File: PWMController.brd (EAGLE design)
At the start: 40 x 30 mm, 13 parts, among them IC1 LM555_DIP, Q1 BC337-25

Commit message: Adding updated files
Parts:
- D1, D2: value 1N4148 -> 1N4148DO35-7; device diode-1:DO35-10 -> diode:DO35-7
- D3: device SparkFun-LED:LED_5MM -> led:LED5MM
- turned J1 to 270 degrees
- turned J3 to 180 degrees
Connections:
- net GND: now also J1.2; no longer J1.1
- net N$1: now also J3.1; no longer J3.3
- net N$4: now also J3.3; no longer J3.1
- net VCC: now also J1.1; no longer J1.2
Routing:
- net V+: track 12.6 -> 14.9 mm
- net N$4: track 7.60 -> 8.87 mm
- net N$1: track 20.1 -> 21.1 mm
- net GND: track 64.9 -> 65.7 mm
- net THRESH_TRIG: track 24.3 -> 25.0 mm

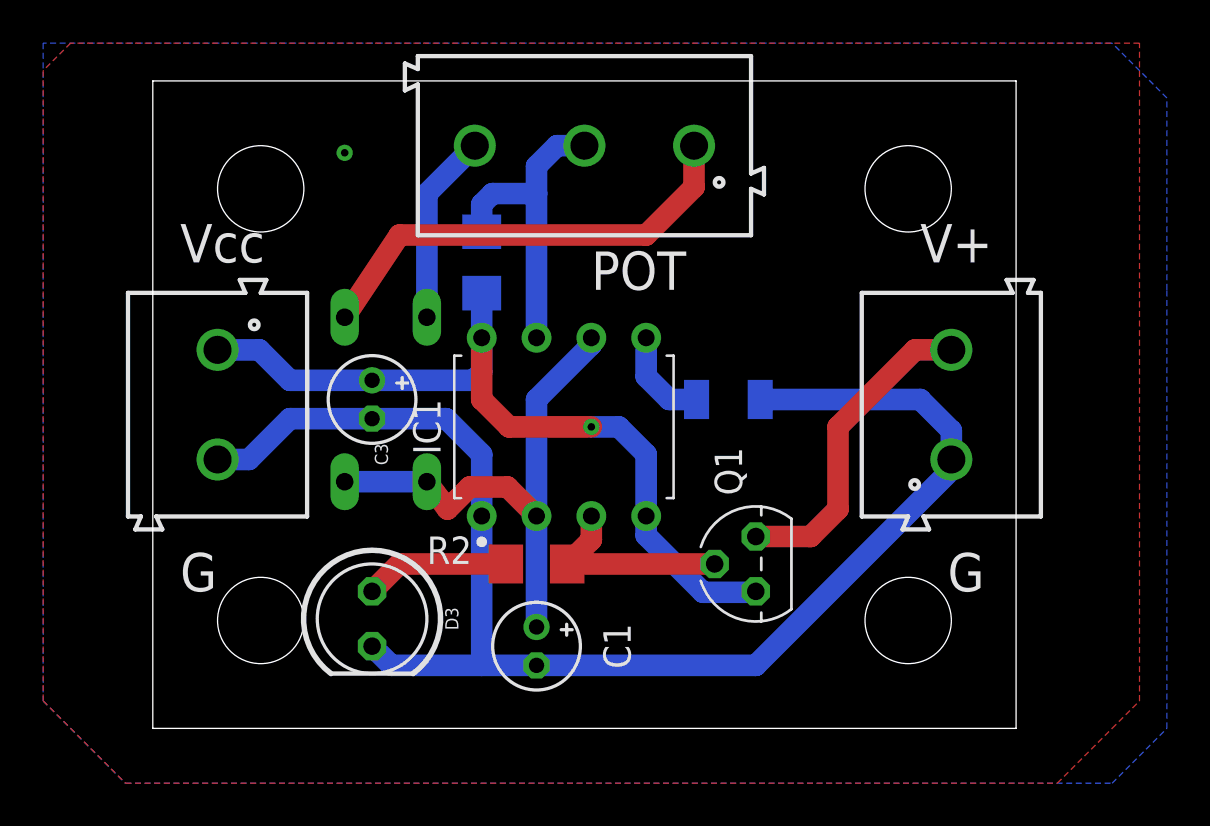
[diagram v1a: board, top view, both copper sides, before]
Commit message: Adding Logo and updating PCB Silkscreen
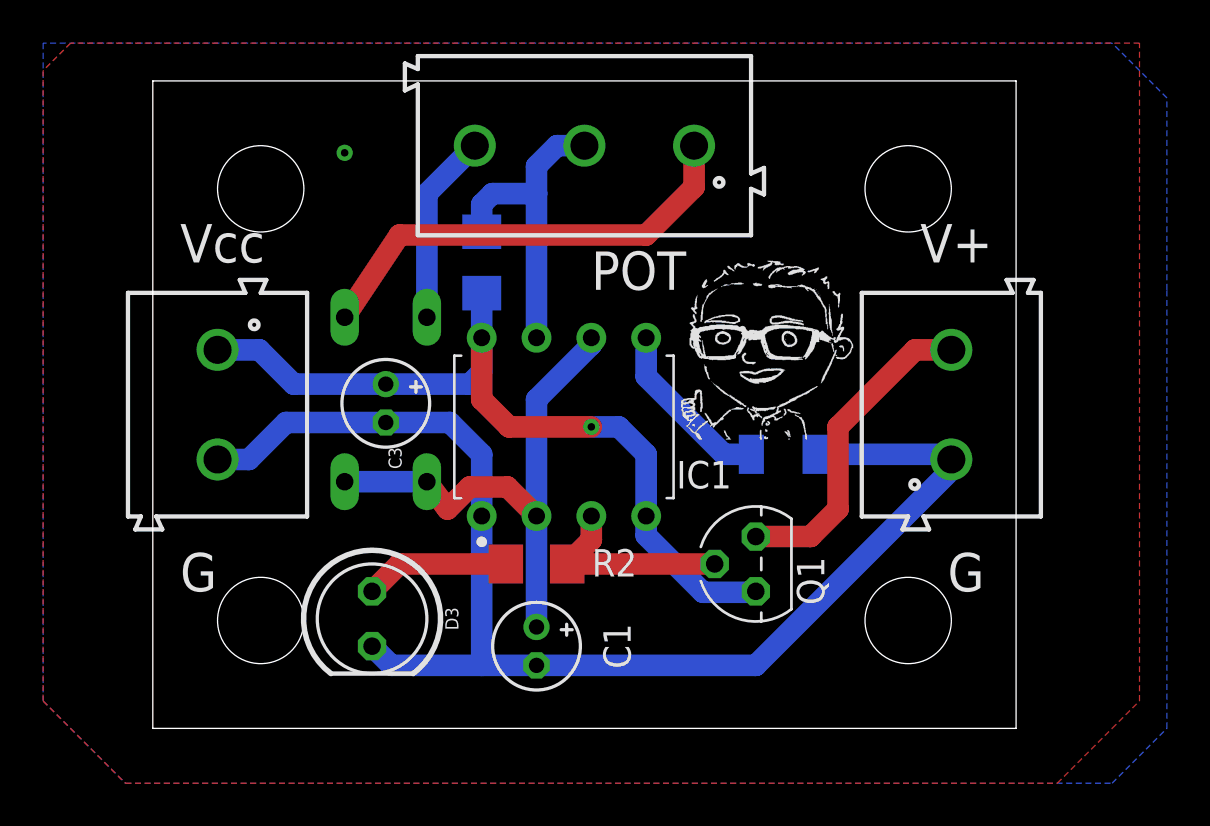
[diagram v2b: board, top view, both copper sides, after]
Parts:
- moved C2 3.59 mm to (29.2, 12.7)
- moved C3 0.66 mm to (10.8, 15.1)
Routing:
- net GND: track 65.7 -> 61.3 mm
- net CONTROL_VOLTAGE: track 4.57 -> 8.16 mm

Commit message: Adding Schematic components update and populated PCB pictures
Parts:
- C3: value XmF -> 100mF
- R1: value (none) -> 1K
- R2: value (none) -> 10K
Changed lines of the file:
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@@
 <drawing>
 <settings>
-<setting alwaysvectorfont="yes"/>
+<setting alwaysvectorfont="no"/>
 <setting verticaltext="up"/>
 </settings>
@@
 </layers>
 <board>
-<fusionsync huburn="a.YnVzaW5lc3M6bXl1bmk2MjA" projecturn="a.YnVzaW5lc3M6bXl1bmk2MjAjMjAyMDA5MTQzMzI2NDA3MDY" f3durn="urn:adsk.wipprod:dm.lineage:VOEC2GXZQGSNXheeIxZnNA" pcbguid="" lastpulledtime="" lastsyncedchangeguid="" latestrevisionid="251e9c42-c37c-4be8-a029-949f2b5d3850" lastsyncedrevisionid="251e9c42-c37c-4be8-a029-949f2b5d3850" lastboardhashguid="66ea59b7-4b6a-7bb7-88af-ee254c0c8002" lastpushedtime="2020-09-22T18:55:46Z" linktopcb3d="false"/>
+<fusionsync huburn="a.YnVzaW5lc3M6bXl1bmk2MjA" projecturn="a.YnVzaW5lc3M6bXl1bmk2MjAjMjAyMDA5MTQzMzI2NDA3MDY" f3durn="urn:adsk.wipprod:dm.lineage:VOEC2GXZQGSNXheeIxZnNA" pcbguid="" lastpulledtime="" lastsyncedchangeguid="" latestrevisionid="251e9c42-c37c-4be8-a029-949f2b5d3850" lastsyncedrevisionid="251e9c42-c37c-4be8-a029-949f2b5d3850" lastboardhashguid="66ea59b7-4b6a-7bb7-88af-ee254c0c8002" lastpushedtime="2020-09-22T18:55:46Z" linktopcb3d="true"/>
 <plain>
 <wire x1="0" y1="0" x2="40" y2="0" width="0" layer="20"/>
@@
 <attribute name="VOLTAGE_RATING" value="" x="29.21" y="12.7" size="1.778" layer="28" rot="MR180" display="off"/>
 </element>
-<element name="C3" library="rcl" library_urn="urn:adsk.eagle:library:334" package="E1,8-4" package3d_urn="urn:adsk.eagle:package:23336/2" value="XmF" x="10.795" y="15.0622" smashed="yes" rot="R270">
+<element name="C3" library="rcl" library_urn="urn:adsk.eagle:library:334" package="E1,8-4" package3d_urn="urn:adsk.eagle:package:23336/2" value="100mF" x="10.795" y="15.0622" smashed="yes" rot="R270">
 <attribute name="NAME" x="10.922" y="12.5222" size="0.6096" layer="25" font="vector" ratio="20" rot="R270" align="bottom-center"/>
 <attribute name="POPULARITY" value="12" x="10.795" y="15.0622" size="1.778" layer="27" rot="R270" display="off"/>
@@
 <attribute name="VALUE" x="30.48" y="12.065" size="1.27" layer="27" ratio="10" rot="R90"/>
 </element>
-<element name="R1" library="rcl" library_urn="urn:adsk.eagle:library:334" package="R1206" package3d_urn="urn:adsk.eagle:package:23540/2" value="" x="15.24" y="21.59" smashed="yes" rot="MR270">
+<element name="R1" library="rcl" library_urn="urn:adsk.eagle:library:334" package="R1206" package3d_urn="urn:adsk.eagle:package:23540/2" value="1K" x="15.24" y="21.59" smashed="yes" rot="MR270">
 <attribute name="NAME" x="17.78" y="22.86" size="1.27" layer="26" rot="MR270"/>
 <attribute name="POPULARITY" value="41" x="62.23" y="-10.16" size="1.778" layer="28" rot="MR270" display="off"/>
@@
 <attribute name="VALUE" x="17.78" y="22.86" size="1.27" layer="28" rot="MR270"/>
 </element>
-<element name="R2" library="rcl" library_urn="urn:adsk.eagle:library:334" package="R1206" package3d_urn="urn:adsk.eagle:package:23540/2" value="" x="17.78" y="7.62" smashed="yes">
+<element name="R2" library="rcl" library_urn="urn:adsk.eagle:library:334" package="R1206" package3d_urn="urn:adsk.eagle:package:23540/2" value="10K" x="17.78" y="7.62" smashed="yes">
 <attribute name="NAME" x="20.3454" y="7.0358" size="1.27" layer="25"/>
 <attribute name="POPULARITY" value="41" x="54.61" y="-39.37" size="1.778" layer="27" display="off"/>
